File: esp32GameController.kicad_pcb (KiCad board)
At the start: 2 copper layers, 42 x 40 mm, 25 parts, among them IC1 BQ21040DBVT, IC2 ESP-WROOM-32_(16MB), J1 USB_B_Micro, J2 Conn_01x02_Male, J3 Conn_02x06_Odd_Even, Q1 2N2219, Q2 2N2219, U1 WIICHUCK, U2 TPS62202DBV

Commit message: Added Silk Screen
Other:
- board text added: "Batt+"
- board text added: "GND"
- board text added: "Rev1 Keion Bisland 2019"
- board text added: "Thermistor"
- board text added: "WiiChuck Wireless Controller Board"

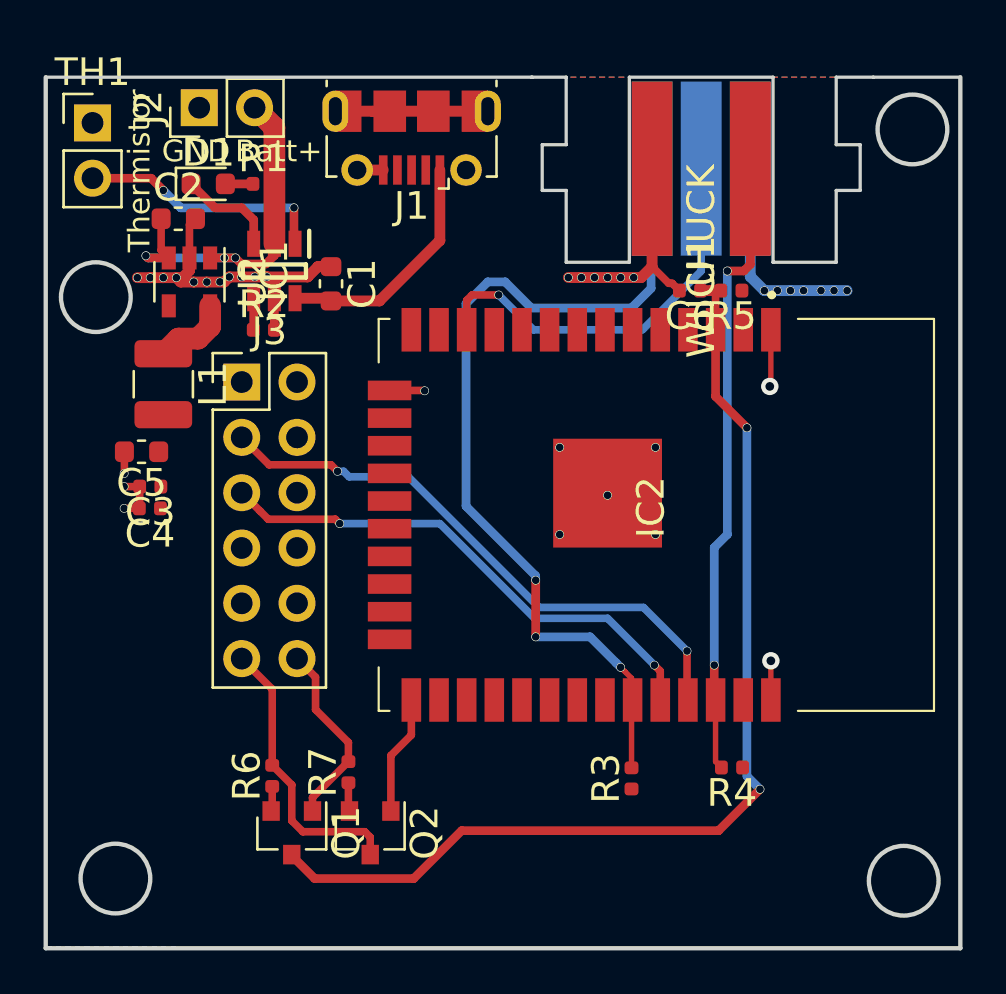
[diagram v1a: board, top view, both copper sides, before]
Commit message: Updated footprint and pinouts
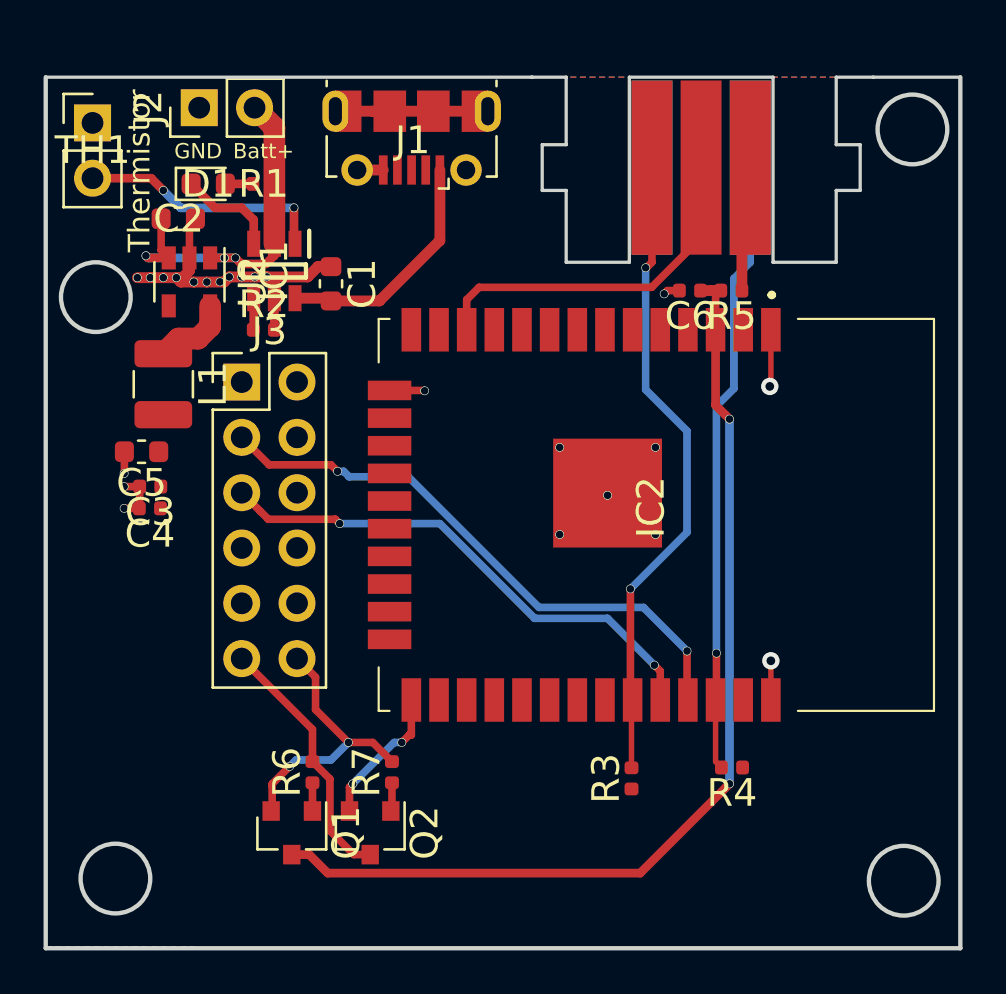
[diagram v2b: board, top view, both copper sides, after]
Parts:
- Q1, Q2: value 2N2219 -> 2N3055
- U1: moved to B.Cu
- moved U1 8.55 mm to (38.1, -0.10), turned to 90 degrees
- moved R7 2.00 mm to (23.9, 31.9)
- moved R6 1.86 mm to (20.2, 31.9)
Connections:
- Q1 pad 1: RTS -> Net-(Q1-Pad1)
- Q1 pad 2: Net-(Q1-Pad2) -> RTS
- Q2 pad 1: IO0 -> Net-(Q2-Pad1)
- Q2 pad 2: Net-(Q2-Pad2) -> IO0
- R6 pad 1: Net-(Q1-Pad2) -> Net-(Q1-Pad1)
- R7 pad 1: Net-(Q2-Pad2) -> Net-(Q2-Pad1)
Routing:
- net SDA: track 41.2 -> 30.6 mm, vias 3 -> 2
- net GND: track 42.4 -> 32.9 mm, vias 28 -> 23
- net RTS: track 8.66 -> 12.7 mm, vias 0 -> 2
- net +3V3: track 9.67 -> 5.81 mm, vias 7 -> 0
- net EN: track 48.4 -> 46.1 mm
- net ATT: track 18.7 -> 16.6 mm, vias 1 -> 0
- net Net-(Q2-Pad2): track 1.32 -> 0.00 mm
- net Net-(Q2-Pad1): track 0.00 -> 1.32 mm
- net Net-(Q1-Pad1): track 0.00 -> 1.30 mm
- net DTR: track 13.1 -> 11.9 mm
- net Net-(Q1-Pad2): track 1.15 -> 0.00 mm
- net IO0: track 5.49 -> 6.61 mm, vias 0 -> 2
- net SCL: track 28.8 -> 28.3 mm, vias 2 -> 1
